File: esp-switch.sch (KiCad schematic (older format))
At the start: 25 parts, among them J1 Screw_Terminal_01x03, J2 Conn_01x04, J4 Conn_01x04, J5 Screw_Terminal_01x02, U1 ATTINY441-SSU, U2 ESP-01v090, U3 MOC3041M, U4 MOC3041M, U5 HLK-PM03

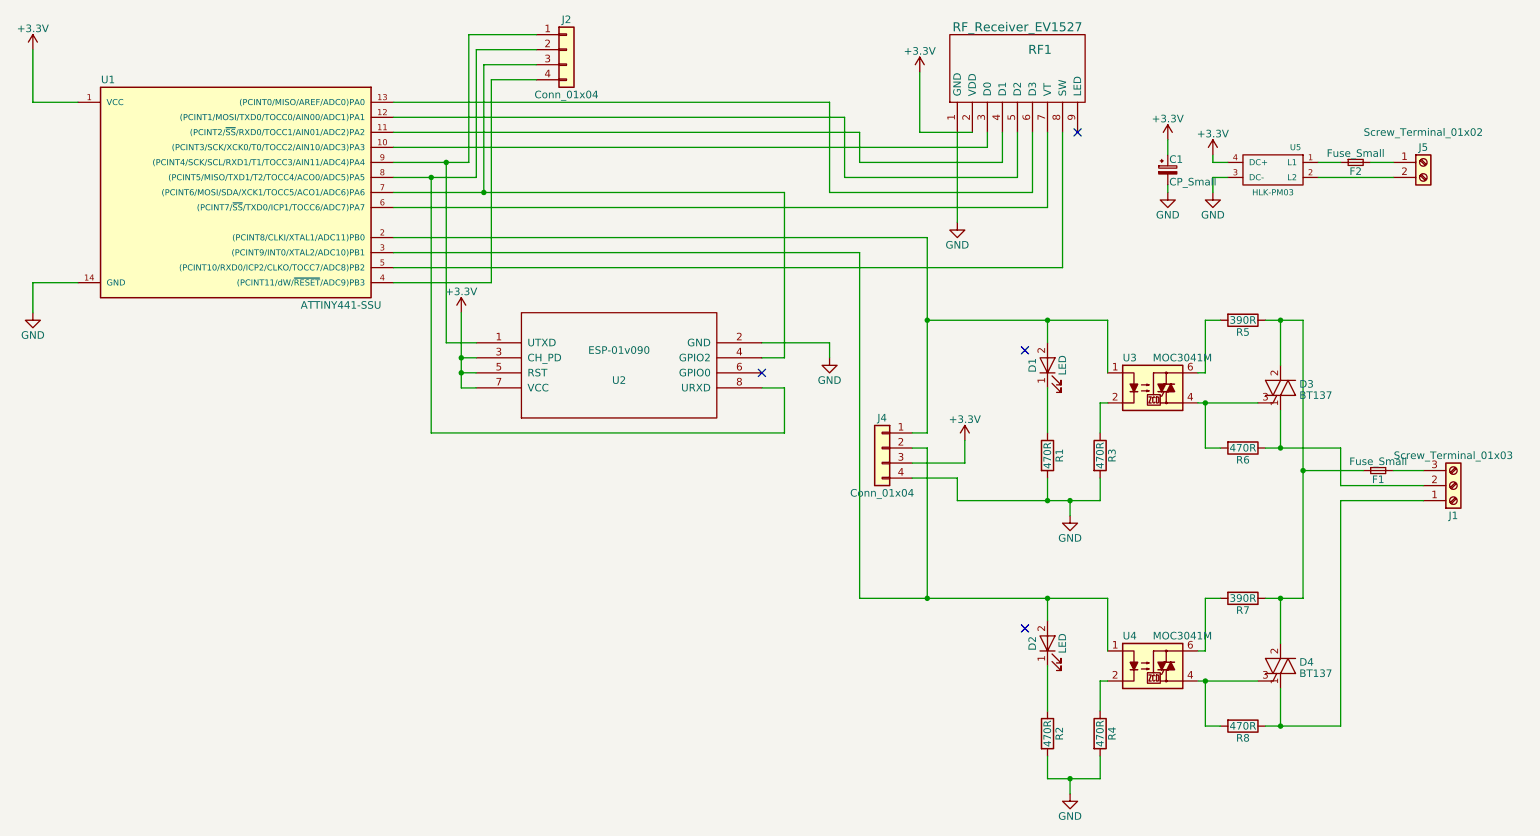
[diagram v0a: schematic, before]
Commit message: V3: mains with shared L and multiple N terminals programming interface for ATTINY moved so can be soldered ATTINY reset available from ESP GPIO0
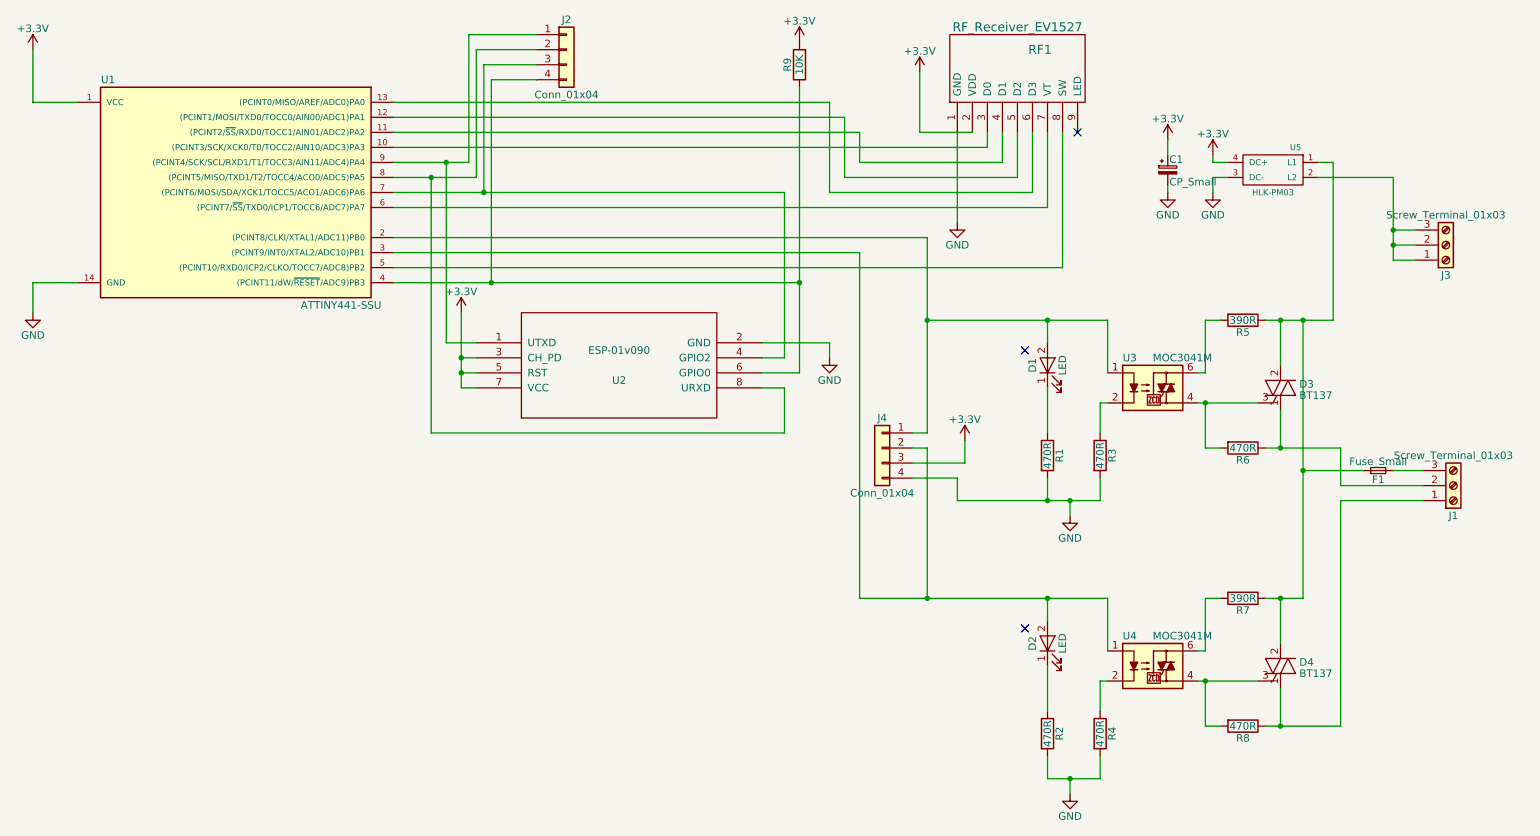
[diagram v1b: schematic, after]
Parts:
- removed F2: Fuse_Small, Resistors_THT:R_Axial_DIN0207_L6.3mm_D2.5mm_P7.62mm_Horizontal, symbol Fuse_Small
- removed J5: Screw_Terminal_01x02, Connectors_Terminal_Blocks:TerminalBlock_Pheonix_MKDS1.5-2pol, symbol Screw_Terminal_01x02
- added J3: Screw_Terminal_01x03, Connectors_Terminal_Blocks:TerminalBlock_Pheonix_MKDS1.5-3pol, symbol Screw_Terminal_01x03
- added R9: 10K, Resistors_THT:R_Axial_DIN0204_L3.6mm_D1.6mm_P2.54mm_Vertical, symbol R
- R1, R2, R3, R4: footprint Resistors_THT:R_Axial_DIN0207_L6.3mm_D2.5mm_P2.54mm_Vertical -> Resistors_THT:R_Axial_DIN0204_L3.6mm_D1.6mm_P2.54mm_Vertical
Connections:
- net +3V3: now also R9.2
- net at J2.4 (Pin_4), U1.4 ((PCINT11/dW/~RESET~/ADC9)PB3): now also U2.6 (GPIO0), R9.1
- net at D3.2 (T2), D4.2 (T2), F1.1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: now also U5.1 (L1)
- net at U5.2 (L2): now also J3.1 (Pin_1), J3.2 (Pin_2), J3.3 (Pin_3)
- no-connect marks 4 -> 3

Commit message: Changed components
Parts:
- D3, D4: value BT137 -> BTA08-600BW
- R3, R4: value 470R -> 150R
- U3, U4: value MOC3041M -> MOC3043M
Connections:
- no-connect marks 3 -> 1
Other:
- note added: "We want to make source current from TINY to be <= 10 mA.\nSo we use MOC3043/MOC3063 - see last '3' here \nstands for modification with trigger current of 5 mA.\nThe Red LED is set up to drain less than 2 mA."
- moved on the sheet: J3
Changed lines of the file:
@@
 P 8650 3000
 F 0 "U3" H 8450 3200 50  0000 L CNN
-F 1 "MOC3041M" H 8650 3200 50  0000 L CNN
+F 1 "MOC3043M" H 8650 3200 50  0000 L CNN
 F 2 "Housings_DIP:DIP-6_W7.62mm" H 8450 2800 50  0001 L CIN
 F 3 "" H 8615 3000 50  0001 L CNN
@@
 	1    0    0    -1
 $EndComp
-NoConn ~ 7800 2750
 $Comp
 L LED D1
@@
 P 8300 3450
 F 0 "R3" V 8380 3450 50  0000 C CNN
-F 1 "470R" V 8300 3450 50  0000 C CNN
+F 1 "150R" V 8300 3450 50  0000 C CNN
 F 2 "Resistors_THT:R_Axial_DIN0204_L3.6mm_D1.6mm_P2.54mm_Vertical" V 8230 3450 50  0001 C CNN
 F 3 "" H 8300 3450 50  0001 C CNN
@@
 P 9500 3000
 F 0 "D3" H 9625 3025 50  0000 L CNN
-F 1 "BT137" H 9625 2950 50  0000 L CNN
+F 1 "BTA08-600BW" H 9625 2950 50  0000 L CNN
 F 2 "TO_SOT_Packages_THT:TO-220_Vertical" V 9575 3025 50  0001 C CNN
 F 3 "" V 9500 3000 50  0001 C CNN
@@
 P 8650 4850
 F 0 "U4" H 8450 5050 50  0000 L CNN
-F 1 "MOC3041M" H 8650 5050 50  0000 L CNN
+F 1 "MOC3043M" H 8650 5050 50  0000 L CNN
 F 2 "Housings_DIP:DIP-6_W7.62mm" H 8450 4650 50  0001 L CIN
 F 3 "" H 8615 4850 50  0001 L CNN
@@
 	1    0    0    -1
 $EndComp
-NoConn ~ 7800 4600
 $Comp
 L LED D2
@@
 P 8300 5300
 F 0 "R4" V 8380 5300 50  0000 C CNN
-F 1 "470R" V 8300 5300 50  0000 C CNN
+F 1 "150R" V 8300 5300 50  0000 C CNN
 F 2 "Resistors_THT:R_Axial_DIN0204_L3.6mm_D1.6mm_P2.54mm_Vertical" V 8230 5300 50  0001 C CNN
 F 3 "" H 8300 5300 50  0001 C CNN
@@
 P 9500 4850
 F 0 "D4" H 9625 4875 50  0000 L CNN
-F 1 "BT137" H 9625 4800 50  0000 L CNN
+F 1 "BTA08-600BW" H 9625 4800 50  0000 L CNN
 F 2 "TO_SOT_Packages_THT:TO-220_Vertical" V 9575 4875 50  0001 C CNN
 F 3 "" V 9500 4850 50  0001 C CNN
@@
 L Screw_Terminal_01x03 J3
 U 1 1 5AEEDF87
-P 10600 2050
-F 0 "J3" H 10600 2250 50  0000 C CNN
-F 1 "Screw_Terminal_01x03" H 10600 1850 50  0000 C CNN
-F 2 "Connectors_Terminal_Blocks:TerminalBlock_Pheonix_MKDS1.5-3pol" H 10600 2050 50  0001 C CNN
-F 3 "" H 10600 2050 50  0001 C CNN
-	1    10600 2050
+P 10600 1350
+F 0 "J3" H 10600 1550 50  0000 C CNN
+F 1 "Screw_Terminal_01x03" H 10600 1150 50  0000 C CNN
+F 2 "Connectors_Terminal_Blocks:TerminalBlock_Pheonix_MKDS1.5-3pol" H 10600 1350 50  0001 C CNN
+F 3 "" H 10600 1350 50  0001 C CNN
+	1    10600 1350
 	1    0    0    1
 $EndComp
@@
 	9850 1500 9750 1500
 Wire Wire Line
-	10250 1600 10250 2150
-Wire Wire Line
-	10250 1950 10400 1950
-Wire Wire Line
-	10250 2050 10400 2050
-Connection ~ 10250 1950
-Wire Wire Line
-	10250 2150 10400 2150
-Connection ~ 10250 2050
+	10250 1250 10400 1250
+Wire Wire Line
+	10250 1350 10400 1350
+Wire Wire Line
+	10250 1450 10400 1450
 Connection ~ 4250 2300
 Wire Wire Line
@@
 Wire Wire Line
 	6300 1000 6300 2900
+Text Notes 3750 3900 0    60   ~ 0
+We want to make source current from TINY to be <= 10 mA.\nSo we use MOC3043/MOC3063 - see last '3' here \nstands for modification with trigger current of 5 mA.\nThe Red LED is set up to drain less than 2 mA.
+Wire Wire Line
+	10250 1600 10250 1250
+Connection ~ 10250 1350
+Connection ~ 10250 1450
 $EndSCHEMATC

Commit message: V4 schematics
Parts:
- removed D1, D2: LED, LEDs:LED_D3.0mm, symbol LED
- removed J1, J3: Screw_Terminal_01x03, Connectors_Terminal_Blocks:TerminalBlock_Pheonix_MKDS1.5-3pol, symbol Screw_Terminal_01x03
- removed R1, R2: 470R, Resistors_THT:R_Axial_DIN0204_L3.6mm_D1.6mm_P2.54mm_Vertical, symbol R
- added J1, J3: Screw_Terminal_01x02, Connectors_Terminal_Blocks:TerminalBlock_Pheonix_MKDS1.5-2pol, symbol Screw_Terminal_01x02
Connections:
- net at D3.1 (T1), R6.1: now also J1.2 (Pin_2)
- net at D4.1 (T1), R8.1: now also J1.1 (Pin_1)
- net at F1.2: now also J3.1 (Pin_1)
- net at U5.2 (L2): now also J3.2 (Pin_2)
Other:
- moved on the sheet: F1
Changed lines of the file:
@@
-$EndComp
-$Comp
-L LED D1
-U 1 1 5A12EBCD
-P 7950 2850
-F 0 "D1" H 7950 2950 50  0000 C CNN
-F 1 "LED" H 7950 2750 50  0000 C CNN
-F 2 "LEDs:LED_D3.0mm" H 7950 2850 50  0001 C CNN
-F 3 "" H 7950 2850 50  0001 C CNN
-	1    7950 2850
-	0    -1   -1   0
-$EndComp
-$Comp
-L R R1
-U 1 1 5A12ECC7
-P 7950 3450
-F 0 "R1" V 8030 3450 50  0000 C CNN
-F 1 "470R" V 7950 3450 50  0000 C CNN
-F 2 "Resistors_THT:R_Axial_DIN0204_L3.6mm_D1.6mm_P2.54mm_Vertical" V 7880 3450 50  0001 C CNN
-F 3 "" H 7950 3450 50  0001 C CNN
-	1    7950 3450
-	1    0    0    -1
 $EndComp
 $Comp
@@
 $EndComp
 $Comp
-L LED D2
-U 1 1 5A132A92
-P 7950 4700
-F 0 "D2" H 7950 4800 50  0000 C CNN
-F 1 "LED" H 7950 4600 50  0000 C CNN
-F 2 "LEDs:LED_D3.0mm" H 7950 4700 50  0001 C CNN
-F 3 "" H 7950 4700 50  0001 C CNN
-	1    7950 4700
-	0    -1   -1   0
-$EndComp
-$Comp
-L R R2
-U 1 1 5A132A98
-P 7950 5300
-F 0 "R2" V 8030 5300 50  0000 C CNN
-F 1 "470R" V 7950 5300 50  0000 C CNN
-F 2 "Resistors_THT:R_Axial_DIN0204_L3.6mm_D1.6mm_P2.54mm_Vertical" V 7880 5300 50  0001 C CNN
-F 3 "" H 7950 5300 50  0001 C CNN
-	1    7950 5300
-	1    0    0    -1
-$EndComp
-$Comp
 L R R4
 U 1 1 5A132A9E
@@
 L GND #PWR05
 U 1 1 5A132AA4
-P 8100 5700
-F 0 "#PWR05" H 8100 5450 50  0001 C CNN
-F 1 "GND" H 8100 5550 50  0000 C CNN
-F 2 "" H 8100 5700 50  0001 C CNN
-F 3 "" H 8100 5700 50  0001 C CNN
-	1    8100 5700
+P 8300 5600
+F 0 "#PWR05" H 8300 5350 50  0001 C CNN
+F 1 "GND" H 8300 5450 50  0000 C CNN
+F 2 "" H 8300 5600 50  0001 C CNN
+F 3 "" H 8300 5600 50  0001 C CNN
+	1    8300 5600
 	1    0    0    -1
 $EndComp
@@
 L Fuse_Small F1
 U 1 1 5A136B02
-P 10150 3550
-F 0 "F1" H 10150 3490 50  0000 C CNN
-F 1 "Fuse_Small" H 10150 3610 50  0000 C CNN
-F 2 "Resistors_THT:R_Axial_DIN0207_L6.3mm_D2.5mm_P7.62mm_Horizontal" H 10150 3550 50  0001 C CNN
-F 3 "" H 10150 3550 50  0001 C CNN
-	1    10150 3550
-	1    0    0    -1
-$EndComp
-$Comp
-L Screw_Terminal_01x03 J1
-U 1 1 5A55A532
-P 10650 3650
-F 0 "J1" H 10650 3850 50  0000 C CNN
-F 1 "Screw_Terminal_01x03" H 10650 3450 50  0000 C CNN
-F 2 "Connectors_Terminal_Blocks:TerminalBlock_Pheonix_MKDS1.5-3pol" H 10650 3650 50  0001 C CNN
-F 3 "" H 10650 3650 50  0001 C CNN
-	1    10650 3650
-	1    0    0    1
-$EndComp
-$Comp
-L Screw_Terminal_01x03 J3
-U 1 1 5AEEDF87
-P 10600 1350
-F 0 "J3" H 10600 1550 50  0000 C CNN
-F 1 "Screw_Terminal_01x03" H 10600 1150 50  0000 C CNN
-F 2 "Connectors_Terminal_Blocks:TerminalBlock_Pheonix_MKDS1.5-3pol" H 10600 1350 50  0001 C CNN
-F 3 "" H 10600 1350 50  0001 C CNN
-	1    10600 1350
-	1    0    0    1
+P 10050 1500
+F 0 "F1" H 10050 1440 50  0000 C CNN
+F 1 "Fuse_Small" H 10050 1560 50  0000 C CNN
+F 2 "Resistors_THT:R_Axial_DIN0207_L6.3mm_D2.5mm_P7.62mm_Horizontal" H 10050 1500 50  0001 C CNN
+F 3 "" H 10050 1500 50  0001 C CNN
+	1    10050 1500
+	1    0    0    -1
 $EndComp
 $Comp
@@
 	4150 3000 4050 3000
 Wire Wire Line
-	7950 3600 7950 3750
-Wire Wire Line
 	7350 3750 8300 3750
 Wire Wire Line
@@
 Connection ~ 8100 3750
 Wire Wire Line
-	7950 3000 7950 3300
-Wire Wire Line
 	8300 3300 8300 3100
 Wire Wire Line
@@
 	8300 3100 8350 3100
 Wire Wire Line
-	7950 2700 7950 2550
-Connection ~ 7950 2550
-Wire Wire Line
 	9350 3100 8950 3100
 Wire Wire Line
@@
 Connection ~ 9500 2550
 Wire Wire Line
-	7950 5450 7950 5600
-Wire Wire Line
-	7950 5600 8300 5600
-Wire Wire Line
 	8300 5600 8300 5450
-Wire Wire Line
-	8100 5600 8100 5700
-Connection ~ 8100 5600
-Wire Wire Line
-	7950 4850 7950 5150
 Wire Wire Line
 	8300 5150 8300 4950
@@
 	8300 4950 8350 4950
 Wire Wire Line
-	7950 4550 7950 4400
-Connection ~ 7950 4400
-Wire Wire Line
 	9350 4950 8950 4950
 Wire Wire Line
@@
 Wire Wire Line
 	7350 3600 7350 3750
-Connection ~ 7950 3750
 Wire Wire Line
 	7050 3500 7400 3500
@@
 Wire Wire Line
 	9650 2550 9650 4400
-Wire Wire Line
-	10050 3550 9650 3550
-Connection ~ 9650 3550
-Wire Wire Line
-	10250 3550 10450 3550
 Wire Wire Line
 	9900 3400 9900 3650
@@
 Connection ~ 9650 2550
 Wire Wire Line
-	9850 1500 9750 1500
-Wire Wire Line
-	10250 1250 10400 1250
-Wire Wire Line
-	10250 1350 10400 1350
-Wire Wire Line
-	10250 1450 10400 1450
+	9750 1500 9950 1500
 Connection ~ 4250 2300
 Wire Wire Line
@@
 Text Notes 3750 3900 0    60   ~ 0
 We want to make source current from TINY to be <= 10 mA.\nSo we use MOC3043/MOC3063 - see last '3' here \nstands for modification with trigger current of 5 mA.\nThe Red LED is set up to drain less than 2 mA.
-Wire Wire Line
-	10250 1600 10250 1250
-Connection ~ 10250 1350
-Connection ~ 10250 1450
+$Comp
+L Screw_Terminal_01x02 J3
+U 1 1 5E7855C3
+P 10450 1500
+F 0 "J3" H 10450 1600 50  0000 C CNN
+F 1 "Screw_Terminal_01x02" H 10450 1300 50  0000 C CNN
+F 2 "Connectors_Terminal_Blocks:TerminalBlock_Pheonix_MKDS1.5-2pol" H 10450 1500 50  0001 C CNN
+F 3 "" H 10450 1500 50  0001 C CNN
+	1    10450 1500
+	1    0    0    -1
+$EndComp
+Connection ~ 9850 1500
+Wire Wire Line
+	10250 1500 10150 1500
+$Comp
+L Screw_Terminal_01x02 J1
+U 1 1 5E786F25
+P 10650 3750
+F 0 "J1" H 10650 3850 50  0000 C CNN
+F 1 "Screw_Terminal_01x02" H 10650 3550 50  0000 C CNN
+F 2 "Connectors_Terminal_Blocks:TerminalBlock_Pheonix_MKDS1.5-2pol" H 10650 3750 50  0001 C CNN
+F 3 "" H 10650 3750 50  0001 C CNN
+	1    10650 3750
+	1    0    0    1
+$EndComp
 $EndSCHEMATC
